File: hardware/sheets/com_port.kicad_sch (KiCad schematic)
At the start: 28 parts, among them J1 DE9_Pins, J2 Conn_01x03, J3 Conn_01x04, U1 16550, U2 MAX3241, U3 74HCT04, U4 74HCT08, U5 74HCT08, U6 74HCT125, Y1 1.8432MHz

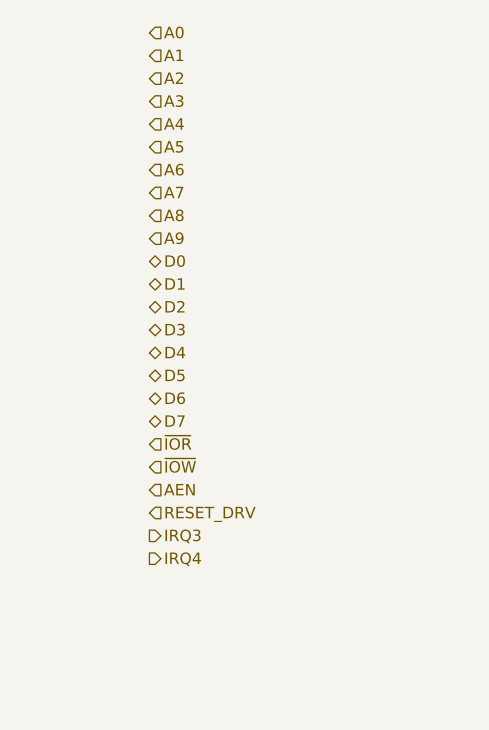
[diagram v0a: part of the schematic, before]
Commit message: ERC cleanup: NC flags on unused pins, anchored interface labels
KiCad 10 ERC drops from 366 to 16 violations, all noise:

- NC flags on the 36 genuinely unused pins (cpu_core '138/'161 spares,
  Supervisor RP2040 unused GPIO, Core2350B GPIO44-47, rtc '138 spares).
- emit_interface anchors every hier label on a stub wire ending in a
  same-name local label -- connectivity unchanged (still by name;
  netlist spans verified), but nothing dangles.
- Interface honesty: cpu_core drops AEN/IOCHRDY from PINS (both live on
  bus_mcu; nothing here touched them), bus_mcu drops PRIV_COUNTER (the
  counter chain is on-sheet, CNT_* never crosses).
- Remaining 6 label_dangling are root IRQ9-13/15: single-sheet by
  design (soft-PIC pull-ups await future 16-bit sources); kept in PINS
  as the AT-style contract.

Co-Authored-By: Claude Fable 5 <noreply@anthropic.com>
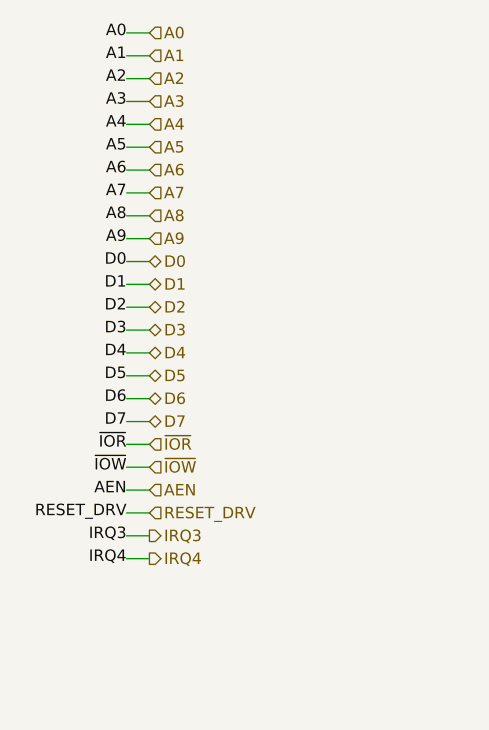
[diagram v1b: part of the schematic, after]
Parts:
- removed C3: 47nF, symbol Device:C
- removed R2: 10k, symbol Device:R
- removed Y1: 1.8432MHz, symbol Device:Crystal
- added C12: 100nF, symbol Device:C
- added JP1: Conn_01x03, symbol Connector_Generic:Conn_01x03
- added U4: 74HCT08, symbol mini-xt:74HCT08
- C3: renamed from JP1; value Conn_01x03 -> 47nF; symbol Connector_Generic:Conn_01x03 -> Device:C; LCSC Part Num C2337 -> C1622
- R2: renamed from C12; value 100nF -> 10k; symbol Device:C -> Device:R; LCSC Part Num C14663 -> C25804
- Y1: renamed from U4; value 74HCT08 -> 1.8432MHz; symbol mini-xt:74HCT08 -> Device:Crystal; LCSC Part Num C5959 -> C47345430
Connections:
- net +5V: now also C12.1, U4.14 (VCC); no longer Y1.14 (VCC)
- net A3: now also U4.1 (P1); no longer Y1.1 (P1)
- net A4: now also U4.2 (P2); no longer Y1.2 (P2)
- net A5: now also U4.4 (P4); no longer Y1.4 (P4)
- net A6: now also U4.5 (P5); no longer Y1.5 (P5)
- net A7: now also U4.9 (P9); no longer Y1.9 (P9)
- net A8_SEL: now also U4.12 (P12); no longer Y1.12 (P12)
- net A9: now also U4.10 (P10); no longer Y1.10 (P10)
- net AEN_N: now also U4.13 (P13); no longer Y1.13 (P13)
- net AND1: now also U4.3 (P3); no longer Y1.3 (P3)
- net AND2: now also U4.6 (P6); no longer Y1.6 (P6)
- net AND3: now also U4.8 (P8); no longer Y1.8 (P8)
- net AND4: now also U4.11 (P11); no longer Y1.11 (P11)
- net BAUD_XI: now also Y1.1
- net BAUD_XO: now also Y1.2
- net C1N: now also C3.2
- net C1P: now also C3.1
- net CONSOLE_RXI: now also JP1.3 (Pin_3); no longer C3.3 (Pin_3)
- net GND: now also C12.2, U4.7 (GND); no longer R2.2, Y1.7 (GND)
- net RXD_RS232: now also JP1.1 (Pin_1); no longer C3.1 (Pin_1)
- net UART_RXD: now also R2.2, JP1.2 (Pin_2); no longer C3.2 (Pin_2)

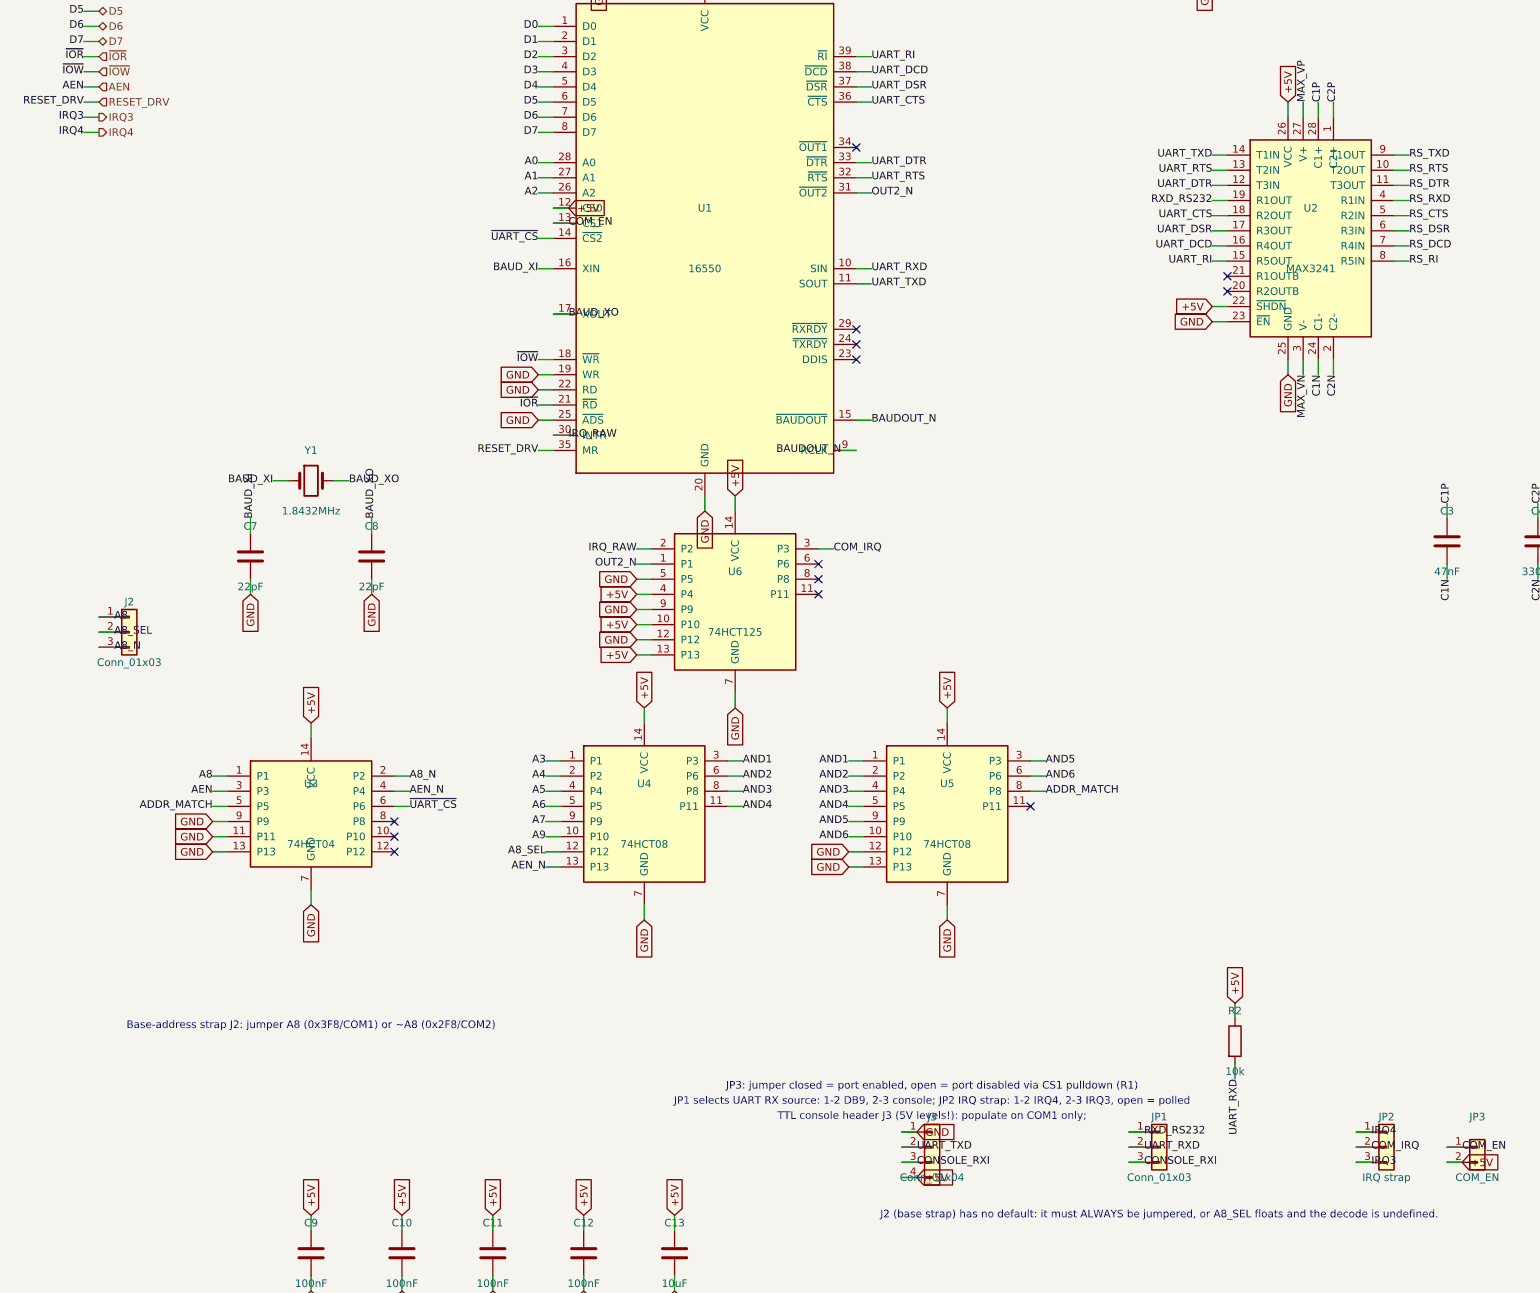
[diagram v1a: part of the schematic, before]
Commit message: IRQ rework: single-'165 collector, hardwired COM/LPT IRQs
- IRQ collector shrunk to one 74HCT165: D0-D6 = IRQ2-8, D7 = IRQ14
  (replacing the source-less IRQ9). U19 + pull-downs R19-R24 + C18
  deleted; IRQ9-13/15 dropped everywhere (nothing on the board or the
  8-bit header can drive them). Firmware shifts 8 bits, Q7-first.
- COM/LPT IRQ straps deleted, hardwired to the PC conventions:
  COM1=IRQ4, COM2=IRQ3 (COM_IRQ per-instance netmap remap -- first use
  of the INSTANCES netmap), LPT=IRQ7 (U13 '125 drives the net
  directly). The enable jumpers (COM JP3, LPT JP2) free an IRQ by
  disabling the port; the tri-state drivers go silent with it.
- Storage JP3 (IRQ14/IRQ5) kept: both positions are real conventions
  (AT vs XT), not conflict avoidance. Its IRQ5 warning now points at
  the PicoGUS jumper block, the only remaining IRQ5 contention.
- Design doc: fix stale claim that IRQ8 rides a reclaimed header pin
  (that pin is a ground return; IRQ8 is motherboard-internal).

Full-build ERC: 0 violations.

Co-Authored-By: Claude Fable 5 <noreply@anthropic.com>
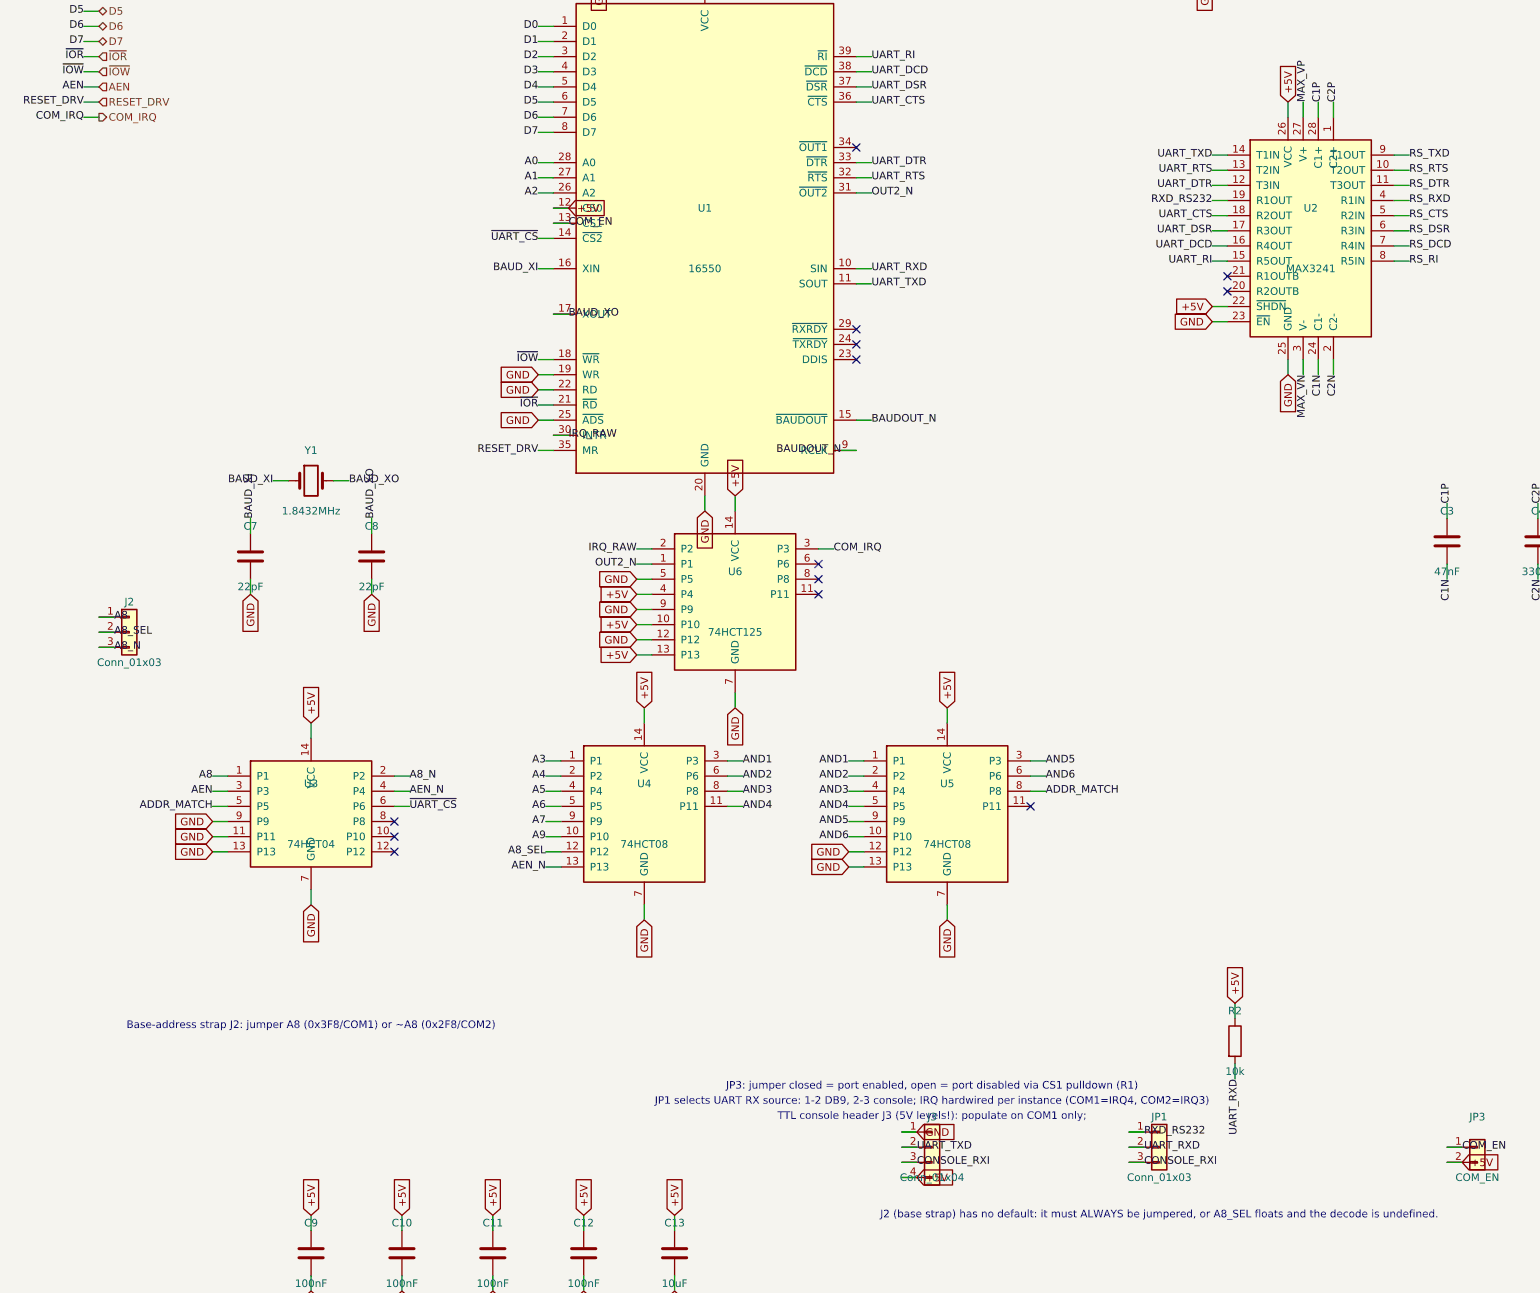
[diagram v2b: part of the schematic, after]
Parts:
- removed C12: 100nF, symbol Device:C
- removed C13: 10uF, symbol Device:C
- removed JP2: IRQ strap, symbol Connector_Generic:Conn_01x03
- added C1, C2: 100nF, symbol Device:C
- C13: renamed from C11; value 100nF -> 10uF; LCSC Part Num C14663 -> C15850
- renumbered C2 to C10, C9 to C11, C10 to C12, C1 to C9
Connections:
- net +5V: now also C1.1, C2.1
- net GND: now also C1.2, C2.2
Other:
- note added: "JP1 selects UART RX source: 1-2 DB9, 2-3 console; IRQ hardwired per instance (COM1=IRQ4, COM2=IRQ3)"
- note removed: "JP1 selects UART RX source: 1-2 DB9, 2-3 console; JP2 IRQ strap: 1-2 IRQ4, 2-3 IRQ3, open = polled"
- moved on the sheet: C10, C11, C12, C13, C9

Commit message: Parts: footprints for all components, close 6 LCSC map gaps, check_parts.py
- mxsch.py emits the Footprint property from component props (was
  hard-coded empty); parts.py entries now carry a verified KiCad
  footprint, applied at build time alongside the LCSC number.
- Map keys fixed to match placed values: USB_PROG, SS34, LED (PicoGUS),
  APS6404L, CB3T3257/45 -- every combo across all sheets + cards now
  resolves (130 combos, 455 netlist components, all with footprints).
- Package corrections from JLC DB re-check: RTL8019AS is QFP-100 14x20
  P0.65 (not TQFP); C2897411 female header is a 2x10 strip -- fine for
  Core2350B, Pico needs 2x 1x20 (noted in jlcpcb-sourcing.md).
- 10 mini-xt:* placeholder footprints mark parts whose land pattern is
  authored at layout from the EasyEDA data (CH224K, magnetics, RJ45,
  HDMI, CF socket, ISA slot, switches, Core2350B PGA).
- New tools/check_parts.py: fails on unmapped combos, missing fp
  fields, or footprints absent from the installed KiCad libs.

Co-Authored-By: Claude Fable 5 <noreply@anthropic.com>
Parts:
- C1, C10, C11, C12, C2, C3, C4, C5, C6, C7, C8, C9: footprint (none) -> Capacitor_SMD:C_0603_1608Metric
- C13: footprint (none) -> Capacitor_SMD:C_0805_2012Metric
- J1: footprint (none) -> Connector_Dsub:DSUB-9_Pins_Horizontal_P2.77x2.84mm_EdgePinOffset9.90mm_Housed_MountingHolesOffset11.32mm
- J2, JP1: footprint (none) -> Connector_PinHeader_2.54mm:PinHeader_1x03_P2.54mm_Vertical
- J3: footprint (none) -> Connector_PinHeader_2.54mm:PinHeader_1x04_P2.54mm_Vertical
- JP3: footprint (none) -> Connector_PinHeader_2.54mm:PinHeader_1x02_P2.54mm_Vertical
- R1, R2: footprint (none) -> Resistor_SMD:R_0603_1608Metric
- U1: footprint (none) -> Package_LCC:PLCC-44_SMD-Socket
- U2: footprint (none) -> Package_SO:SSOP-28_5.3x10.2mm_P0.65mm
- U3, U4, U5, U6: footprint (none) -> Package_SO:SOIC-14_3.9x8.7mm_P1.27mm
- Y1: footprint (none) -> Crystal:Crystal_HC49-U_Vertical
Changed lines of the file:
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@@
 			)
 		)
-		(property "Footprint" ""
+		(property "Footprint" "Package_LCC:PLCC-44_SMD-Socket"
 			(at 127 101.6 0)
 			(effects
@@
 			)
 		)
-		(property "Footprint" ""
+		(property "Footprint" "Crystal:Crystal_HC49-U_Vertical"
 			(at 60.96 142.24 0)
 			(effects
@@
 			)
 		)
-		(property "Footprint" ""
+		(property "Footprint" "Capacitor_SMD:C_0603_1608Metric"
 			(at 50.8 154.94 0)
 			(effects
@@
 			)
 		)
-		(property "Footprint" ""
+		(property "Footprint" "Capacitor_SMD:C_0603_1608Metric"
 			(at 71.12 154.94 0)
 			(effects
@@
 			)
 		)
-		(property "Footprint" ""
+		(property "Footprint" "Package_SO:SOIC-14_3.9x8.7mm_P1.27mm"
 			(at 60.96 198.12 0)
 			(effects
@@
 			)
 		)
-		(property "Footprint" ""
+		(property "Footprint" "Connector_PinHeader_2.54mm:PinHeader_1x03_P2.54mm_Vertical"
 			(at 30.48 167.64 0)
 			(effects
@@
 			)
 		)
-		(property "Footprint" ""
+		(property "Footprint" "Package_SO:SOIC-14_3.9x8.7mm_P1.27mm"
 			(at 116.84 198.12 0)
 			(effects
@@
 			)
 		)
-		(property "Footprint" ""
+		(property "Footprint" "Package_SO:SOIC-14_3.9x8.7mm_P1.27mm"
 			(at 167.64 198.12 0)
 			(effects
@@
 			)
 		)
-		(property "Footprint" ""
+		(property "Footprint" "Package_SO:SOIC-14_3.9x8.7mm_P1.27mm"
 			(at 132.08 162.56 0)
 			(effects
@@
 			)
 		)
-		(property "Footprint" ""
+		(property "Footprint" "Package_SO:SSOP-28_5.3x10.2mm_P0.65mm"
 			(at 228.6 101.6 0)
 			(effects
@@
 			)
 		)
-		(property "Footprint" ""
+		(property "Footprint" "Capacitor_SMD:C_0603_1608Metric"
 			(at 251.46 152.4 0)
 			(effects
@@
 			)
 		)
-		(property "Footprint" ""
+		(property "Footprint" "Capacitor_SMD:C_0603_1608Metric"
 			(at 266.7 152.4 0)
 			(effects
@@
 			)
 		)
-		(property "Footprint" ""
+		(property "Footprint" "Capacitor_SMD:C_0603_1608Metric"
 			(at 281.94 152.4 0)
 			(effects
@@
 			)
 		)
-		(property "Footprint" ""
+		(property "Footprint" "Capacitor_SMD:C_0603_1608Metric"
 			(at 297.18 152.4 0)
 			(effects
@@
 			)
 		)
-		(property "Footprint" ""
+		(property "Footprint" "Connector_Dsub:DSUB-9_Pins_Horizontal_P2.77x2.84mm_EdgePinOffset9.90mm_Housed_MountingHolesOffset11.32mm"
 			(at 330.2 101.6 0)
 			(effects
@@
 			)
 		)
-		(property "Footprint" ""
+		(property "Footprint" "Connector_PinHeader_2.54mm:PinHeader_1x04_P2.54mm_Vertical"
 			(at 165.1 254 0)
 			(effects
@@
 			)
 		)
-		(property "Footprint" ""
+		(property "Footprint" "Connector_PinHeader_2.54mm:PinHeader_1x03_P2.54mm_Vertical"
 			(at 203.2 254 0)
 			(effects
@@
 			)
 		)
-		(property "Footprint" ""
+		(property "Footprint" "Resistor_SMD:R_0603_1608Metric"
 			(at 215.9 236.22 0)
 			(effects
@@
 			)
 		)
-		(property "Footprint" ""
+		(property "Footprint" "Connector_PinHeader_2.54mm:PinHeader_1x02_P2.54mm_Vertical"
 			(at 256.54 254 0)
 			(effects
@@
 			)
 		)
-		(property "Footprint" ""
+		(property "Footprint" "Resistor_SMD:R_0603_1608Metric"
 			(at 271.78 254 0)
 			(effects
@@
 			)
 		)
-		(property "Footprint" ""
+		(property "Footprint" "Capacitor_SMD:C_0603_1608Metric"
 			(at 109.22 50.8 0)
 			(effects
@@
 			)
 		)
-		(property "Footprint" ""
+		(property "Footprint" "Capacitor_SMD:C_0603_1608Metric"
 			(at 210.82 50.8 0)
 			(effects
@@
 			)
 		)
-		(property "Footprint" ""
+		(property "Footprint" "Capacitor_SMD:C_0603_1608Metric"
 			(at 60.96 271.78 0)
 			(effects
@@
 			)
 		)
-		(property "Footprint" ""
+		(property "Footprint" "Capacitor_SMD:C_0603_1608Metric"
 			(at 76.2 271.78 0)
 			(effects
@@
 			)
 		)
-		(property "Footprint" ""
+		(property "Footprint" "Capacitor_SMD:C_0603_1608Metric"
 			(at 91.44 271.78 0)
 			(effects
@@
 			)
 		)
-		(property "Footprint" ""
+		(property "Footprint" "Capacitor_SMD:C_0603_1608Metric"
 			(at 106.68 271.78 0)
 			(effects
@@
 			)
 		)
-		(property "Footprint" ""
+		(property "Footprint" "Capacitor_SMD:C_0805_2012Metric"
 			(at 121.92 271.78 0)
 			(effects

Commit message: Symbols+parts: IS62WV51216, TL16C550CPT, I2C RTC; 3.3V LVC/HC rebinds
New flat mini-xt: symbols (gensym.py), pins verified against
jlc_get_pinout + datasheet (PCF8563 caught a jlc_get_pinout numbering bug):
IS62WV51216 (512Kx16 SRAM, TSOP-44), TL16C550PT (TL16C550C UART, LQFP-48,
NO.PT numbering -- distinct from the old DIP-40 16550 symbol), PCF8563
(I2C RTC, SO-8).

parts.py: bind the three new parts (SRAM in stock at JLC; TL16C550CPT
sourced elsewhere like the V20, 0 JLC stock; PCF8563 + CR2032 holder on
Device:Battery_Cell); rebind the clock dividers to 74LVC74A/74LVC161
(check 7: HC/HCT both fail fmax margin at 3.3V/14.318MHz); add LVC-grade
binds for 5V-tolerant-input octal parts (74LVC573A/244A/574A/125A/245A)
and plain-HC binds for pure-3.3V-domain gates (74HC00/04/32/138) on the
existing HCT-body symbols; add 74LVC2G07 as a value override on the
pin-identical 74LVC2G06 body. Delete the now-dead AS6C4008 DIP-32 socket,
16550 PLCC-44 socket, and DS12C887 DIP-24 socket entries (replaced parts,
no longer sourced).

Sanity build (build.py) still passes: root + 13 sheets, exit 0. The three
deleted entries leave their still-unrewired sheets (cpu_core, com_port,
rtc) temporarily unmapped in check_parts.py until Tasks 4-9 rewire them --
expected transitional state, not a regression.

Co-Authored-By: Claude Fable 5 <noreply@anthropic.com>
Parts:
- U1: footprint Package_LCC:PLCC-44_SMD-Socket -> (none); LCSC Part Num C2828044 -> (none)
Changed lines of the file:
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@@
 			)
 		)
-		(property "Footprint" "Package_LCC:PLCC-44_SMD-Socket"
+		(property "Footprint" ""
 			(at 127 101.6 0)
 			(effects
-				(font
-					(size 1.27 1.27)
-				)
-				(hide yes)
-			)
-		)
-		(property "LCSC Part Num" "C2828044"
-			(at 127 101.6 0)
-			(effects
